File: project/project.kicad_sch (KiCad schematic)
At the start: 30 parts, among them J1 Conn_02x16_Odd_Even, J2 TYPE-C 6P(040新), SW1 SS-12D10L9, U1 DRV8833PWPR, U2 CH224K, U3 DRV8833PWPR, U4 AP63203WU-7, U5 TP4056

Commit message: Step down voltage regulator
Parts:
- removed TP1: TestPoint_2Pole, symbol Connector:TestPoint_2Pole
- added C13, C6: 4.7u, symbol Device:C_Small
- added R3: 10K, symbol Device:R_Small
- added R4: 37.5K, symbol Device:R_Small
- added U6: AP2114, Package_SO:MSOP-8_3x3mm_P0.65mm, symbol Regulator_Linear:MIC5219YMM
- added U7: TPS61099DRV, Package_SON:WSON-6-1EP_2x2mm_P0.65mm_EP1x1.6mm, symbol Regulator_Switching:TPS61099DRV
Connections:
- net 3V3 Out: now also C13.1, R4.1, U6.3 (OUT)
- net Battery: now also SW1.1 (B), C6.1, U6.2 (IN)
- net GND: now also C13.2, C6.2, R3.2, U6.5 (GND), U6.6 (GND), U6.7 (GND), U6.8 (GND)
- net BATT: now reaches SW1.3 (A), TP2.1
- new net: U7.1 (GND), U7.7 (GND)
- new net: R3.1, R4.2, U6.4 (ADJ)
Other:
- note added: "OFF"
- note added: "ON"
- note added: "Step down voltage regulator"
- note added: "Step up voltage regulator"
- note added: "uC Cntrontrolling ON/OFF state"
- moved on the sheet: C1, C10, C11, C12, C2, C3, C4, C5, C7, C8, C9, D1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

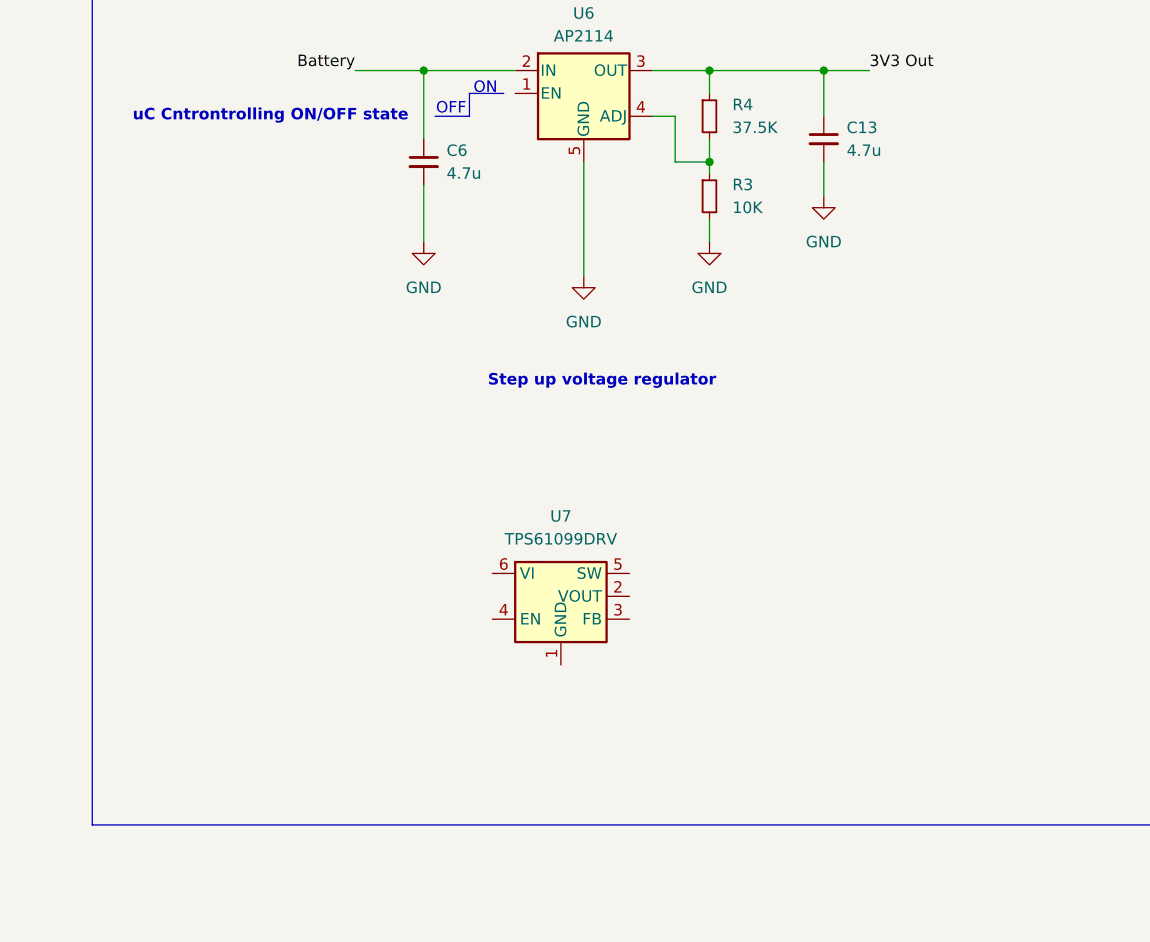
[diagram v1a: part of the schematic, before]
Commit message: Step up voltage regulation
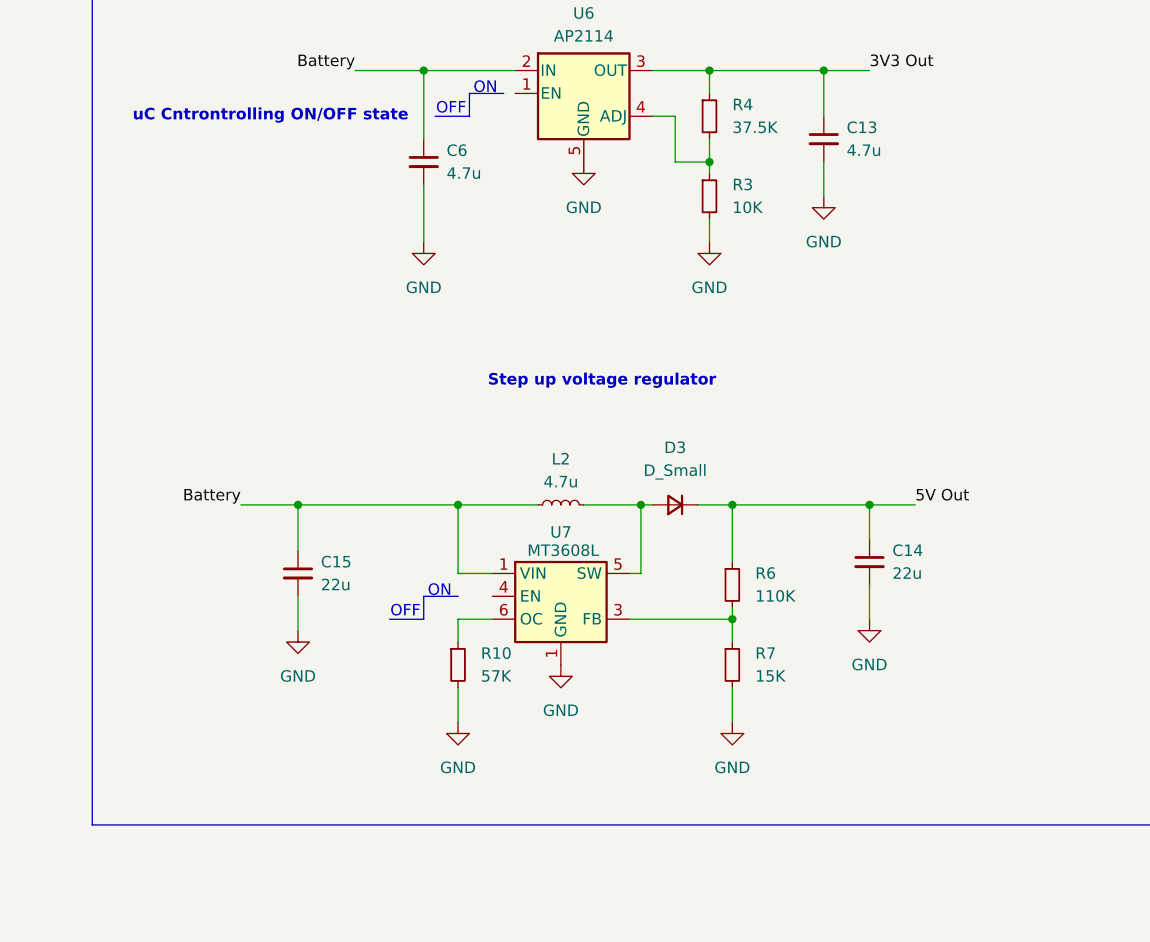
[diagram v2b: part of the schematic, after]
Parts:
- added C14, C15: 22u, symbol Device:C_Small
- added D3: D_Small, symbol Device:D_Small
- added L2: 4.7u, symbol Device:L_Small
- added R10: 57K, symbol Device:R_Small
- added R6: 110K, symbol Device:R_Small
- added R7: 15K, symbol Device:R_Small
- U7: value TPS61099DRV -> MT3608L
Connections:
- net 5V Out: now also C14.1, D3.1 (K), R6.1
- net Battery: now also U7.1 (GND), C15.1, L2.1
- net GND: now also U7.1 (GND), U7.7 (GND), C14.2, C15.2, R10.2, R7.2
- net at U7.3 (FB): now also R6.2, R7.1
- net at U7.5 (SW): now also D3.2 (A), L2.2
- net at U7.6 (OC): now also R10.1

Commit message: Assigning LCSC
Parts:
- J2: LCSC (none) -> TYPE-C 6P(040新)
- SW1: LCSC (none) -> SS-12D10L9
- U2: LCSC (none) -> CH224K
- U6: LCSC (none) -> AP2114H-3.3TRG1
- U7: LCSC (none) -> MT3608L
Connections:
- net VDD is gone; now on net Battery: C1.1, R1.1, U2.1 (VDD)
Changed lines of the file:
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@@
 		)
 	)
+	(label "Battery"
+		(at 387.35 52.07 90)
+		(effects
+			(font
+				(size 1.27 1.27)
+			)
+			(justify left bottom)
+		)
+	)
 	(label "5V Out"
 		(at 306.07 80.01 0)
@@
 		)
 	)
-	(global_label "VDD"
-		(shape input)
-		(at 387.35 52.07 90)
-		(fields_autoplaced yes)
-		(effects
-			(font
-				(size 1.27 1.27)
-			)
-			(justify left)
-		)
-		(property "Intersheetrefs" "${INTERSHEET_REFS}"
-			(at 387.35 45.4562 90)
-			(effects
-				(font
-					(size 1.27 1.27)
-				)
-				(justify left)
-				(hide yes)
-			)
-		)
-	)
 	(global_label "MOTOR3_CTRL2"
 		(shape input)
@@
 			)
 		)
+		(property "LCSC" "SS-12D10L9"
+			(at 369.57 25.4 0)
+			(effects
+				(font
+					(size 1.27 1.27)
+				)
+				(hide yes)
+			)
+		)
 		(pin "3"
 		)
@@
 			)
 		)
+		(property "LCSC" "MT3608L"
+			(at 266.7 92.71 0)
+			(effects
+				(font
+					(size 1.27 1.27)
+				)
+				(hide yes)
+			)
+		)
 		(pin "6"
 		)
@@
 			)
 		)
+		(property "LCSC" "AP2114H-3.3TRG1"
+			(at 269.24 34.29 0)
+			(effects
+				(font
+					(size 1.27 1.27)
+				)
+				(hide yes)
+			)
+		)
 		(pin "2"
 		)
@@
 			)
 		)
+		(property "LCSC" "TYPE-C 6P(040新)"
+			(at 350.52 76.2 0)
+			(effects
+				(font
+					(size 1.27 1.27)
+				)
+				(hide yes)
+			)
+		)
 		(pin "A12"
 		)
@@
 			(at 384.81 86.36 0)
 			(effects
+				(font
+					(size 1.27 1.27)
+				)
+				(hide yes)
+			)
+		)
+		(property "LCSC" "CH224K"
+			(at 384.81 86.36 0)
+			(effects

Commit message: NEW
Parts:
- added BATTER+1, TP10, TP11, TP12, TP13, TP4, TP5, TP6, TP7, TP8, TP9: TestPoint, symbol Connector:TestPoint
- added C16, C17: 1uF, symbol Device:C_Small
- added J3: Conn_01x02_Pin, symbol Connector:Conn_01x02_Pin
- added R14, R5: 10k, symbol Device:R_Small
- added R8: 4.7k, Resistor_SMD:R_0402_1005Metric_Pad0.72x0.64mm_HandSolder, symbol Device:R_Small
- added R9: 4.7k, symbol Device:R_Small
- added U10, U9: TPS22965DSGR, TPS22965DSGR:SON50P200X200X80-9N, symbol TPS22965DSGR:TPS22965DSGR
- added U8: INA219AIDCNR, INA219AIDCNR:SOT65P280X145-8N, symbol INA219:INA219AIDCNR
- U1: LCSC (none) -> C50506
- renumbered R5 to R11, R8 to R12, R9 to R13
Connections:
- net 5V Out: now also C16.1, C17.1, U10.1 (VIN), U10.2 (VIN), U10.4 (VBIAS), U9.1 (VIN), U9.2 (VIN), U9.4 (VBIAS)
- net BATT: now also C11.1, U5.5 (BAT), BATTER+1.1, J3.1 (Pin_1), TP4.1, U8.1 (IN+)
- net CTRL_EXT_LOAD1: now also U10.3 (ON), U9.3 (ON)
- net EXT_LOAD1_OUT: now also R14.1, R5.1, U10.7 (VOUT), U10.8 (VOUT), U9.7 (VOUT), U9.8 (VOUT)
- net GND: now also C16.2, C17.2, J3.2 (Pin_2), R14.2, R5.2, U10.5 (GND), U10.9 (GND), U10.9_1 (GND), U10.9_2 (GND), U8.3 (GND), U8.8 (A1), U9.5 (GND), U9.9 (GND), U9.9_1 (GND), U9.9_2 (GND)
- net I2C1_SCL: now also R8.2, U8.5 (SCL)
- net I2C1_SDA: now also R9.2, U8.6 (SDA)
- net MOTOR1_A_OUT: now also TP10.1
- net MOTOR1_B_OUT: now also TP11.1
- net MOTOR2_A_OUT: now also TP12.1
- net MOTOR2_B_OUT: now also TP13.1
- net MOTOR3_A_OUT: now also TP6.1
- net MOTOR3_B_OUT: now also TP7.1
- net MOTOR4_A_OUT: now also TP8.1
- net MOTOR4_B_OUT: now also TP9.1
- net at C10.1, D1.2 (A), D2.2 (A)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: now also TP5.1
- new net 3V3: R8.1, R9.1, U8.4 (VS), U8.7 (A0)
- new net BATT-: U8.2 (IN-)
- no-connect marks 5 -> 7
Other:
- note added: "Charge the battery from the 9V input pin"
- note added: "Motor driver"
- note added: "Provide 2x External Load Switching at 1A each"
- moved on the sheet: C10, C11, C12, C2, C3, C4, C5, C7, C8, C9, D1, D2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

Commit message: CHANGED RESISTOR VALUE
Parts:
- R8: value 4.7k -> 3.7k
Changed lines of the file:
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@@
 			)
 		)
-		(property "Value" "4.7k"
+		(property "Value" "3.7k"
 			(at 68.58 95.2499 0)
 			(effects
